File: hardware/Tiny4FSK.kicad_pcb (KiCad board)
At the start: 4 copper layers, 18 x 63 mm, 88 parts, among them J10 GPIO_ROW, J2 PWR, J7 GCT-4105, J8 SWD, J9 Counterpoise, SW1 PWR, SW2 RST, U1 BME280, U10 USBLC6-2SC6, U11 ATGM336H, U3 TPS61200DRC, U5 ATSAMD21G18A-A, U6 Si4463, U7 XC6210B332MR, U9 TPS2116DRL

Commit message: more layout progress
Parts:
- moved C30 6.01 mm to (145.6, 97.1)
- moved U2 5.48 mm to (143.8, 96.7), turned to 90 degrees
- moved AE1 3.29 mm to (146.1, 65.9), turned to 180 degrees
- moved R7 0.64 mm to (147.8, 86.1), turned to 135 degrees
- moved J7 0.55 mm to (145.9, 103.5)
- moved L8 0.52 mm to (151.8, 65.9)
- moved R22 0.50 mm to (147.9, 96.8), turned to 45 degrees
- moved R8 0.45 mm to (156.1, 87.5), turned to -135 degrees
- moved U8 0.40 mm to (150.6, 110.5)
- moved C26 0.40 mm to (150.6, 112.4)
- moved R9 0.29 mm to (155.4, 86.8)
- moved C9 0.11 mm to (146.5, 87.4)
- moved C11 0.11 mm to (147.1, 86.8)
- moved C37 0.06 mm to (144.6, 93.5)
- moved R21 0.06 mm to (145.3, 94.2)

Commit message: draft of routing
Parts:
- removed J9: Counterpoise, Connector_PinHeader_2.54mm:PinHeader_1x01_P2.54mm_Vertical
- moved H2 50.2 mm to (158.8, 120.8)
- moved H1 17.6 mm to (158.8, 70.2)
- moved C34 8.72 mm to (152.6, 114.4)
- moved C35 8.72 mm to (151.7, 114.4)
- moved C25 7.37 mm to (150.2, 115.1), turned to 0 degrees
- moved U9 4.21 mm to (149.9, 113.2), turned to -90 degrees
- moved C19 3.79 mm to (147.6, 112.1), turned to 180 degrees
- moved C26 3.33 mm to (148.4, 109.9), turned to 90 degrees
- moved AE1 3.22 mm to (144.1, 68.4), turned to -90 degrees
- moved L3 2.18 mm to (156.6, 112.2)
- moved R5 1.14 mm to (151.2, 101.0)
- moved C18 1.13 mm to (156.4, 97.8)
- moved C17 1.03 mm to (151.3, 98.6)
- moved U7 1.03 mm to (153.9, 99.1)
- moved U10 1.01 mm to (153.8, 102.5)
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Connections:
- C27 pad 2: /radio/SI_TX -> Net-(C16-Pad2)
- J10 pad 10: /interface/GP.GPIO13 -> /interface/GP.GPIO10
- J10 pad 11: /interface/GP.GPIO38 -> /interface/GP.GPIO12
- J10 pad 13: /interface/GP.GPIO_A_1 -> /interface/GP.SCL
- J10 pad 14: /interface/GP.GPIO_A_2 -> /interface/GP.SDA
- J10 pad 2: /interface/GP.SDA -> /interface/GP.GPIO_A_1
- J10 pad 3: /interface/GP.SCL -> /interface/GP.GPIO_A_2
- J10 pad 9: /interface/GP.GPIO12 -> /interface/GP.GPIO13
- J2 pad 2: +BATT -> +3.3V
- J2 pad 6: +3.3V -> +BATT
- L10 pad 2: /radio/SI_TX -> Net-(C16-Pad2)
- U5 pad 11: /mcu/GPS.EN -> /mcu/SI.SDN
- U5 pad 13: /interface/LED.SUCCESS -> /interface/GP.~{CS}
- U5 pad 14: /mcu/SI_CTL.GP1 -> /mcu/SI.GP1
- U5 pad 22: /interface/GP.GPIO38 -> /mcu/SI.GP0
- U5 pad 23: /mcu/SI.GP0 -> unconnected-(U5-PA14-Pad23)
- U5 pad 24: /interface/LED.ERROR -> unconnected-(U5-PA15-Pad24)
- U5 pad 25: /mcu/SI.SDN -> unconnected-(U5-PA16-Pad25)
- U5 pad 27: /interface/GP.~{CS} -> /interface/GP.GPIO10
- U5 pad 39: unconnected-(U5-PA27-Pad39) -> /mcu/GPS.EN
- U5 pad 47: unconnected-(U5-PB02-Pad47) -> /interface/LED.SUCCESS
- U5 pad 48: unconnected-(U5-PB03-Pad48) -> /interface/LED.ERROR
- U6 pad 14: /interface/GP.MISO -> /interface/GP.MOSI
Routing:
- net +BATT: track 0.00 -> 60.7 mm, vias 0 -> 6
- net /interface/PROG.~{RESET}: track 0.00 -> 52.1 mm, vias 0 -> 2
- net /interface/GP.GPIO_A_1: track 0.00 -> 40.9 mm, vias 0 -> 1
- net /interface/GP.GPIO_A_2: track 0.00 -> 39.1 mm, vias 0 -> 1
- net /interface/LED.SUCCESS: track 0.00 -> 38.6 mm, vias 0 -> 2
- net /interface/LED.ERROR: track 0.00 -> 37.1 mm, vias 0 -> 2
- net +3.3V: track 0.00 -> 36.7 mm, vias 0 -> 24
- net /interface/GP.SDA: track 0.00 -> 26.0 mm, vias 0 -> 1
- net /interface/GP.SCL: track 0.00 -> 24.6 mm
- net /power/USB_3V3: track 0.00 -> 23.9 mm, vias 0 -> 3
- net /interface/GP.MISO: track 0.00 -> 22.9 mm, vias 0 -> 3
- net /interface/GP.MOSI: track 0.00 -> 22.6 mm, vias 0 -> 2
- net /power/USB_VBUS: track 0.00 -> 21.7 mm, vias 0 -> 9
- net /interface/GP.D+: track 0.00 -> 21.5 mm, vias 0 -> 2
- net /power/BST_IN: track 0.00 -> 20.2 mm, vias 0 -> 5
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- added copper zone on F.Cu, net +3.3V
- added copper zone on In2.Cu, net +3.3V
- added copper zone on In2.Cu, net /power/BATT_3V3
- added copper zone on F.Cu, net /power/BST_IN
- added copper zone on In2.Cu, net /power/USB_VBUS
- added copper zone on B.Cu, net Earth
- added copper zone on F.Cu, net Earth
- added copper zone on In1.Cu, net Earth
- added copper zone on F.Cu, net Net-(U3-L)

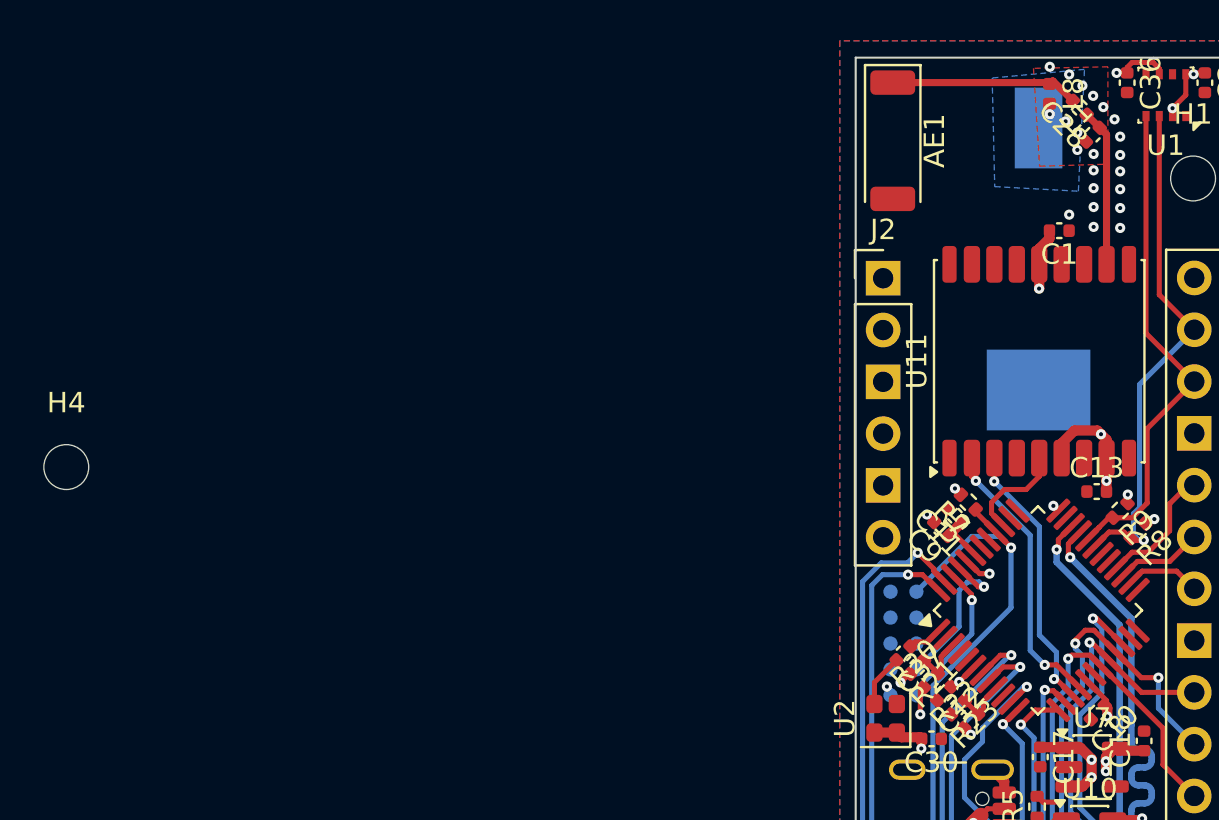
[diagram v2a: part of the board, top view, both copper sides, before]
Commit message: fix footprints
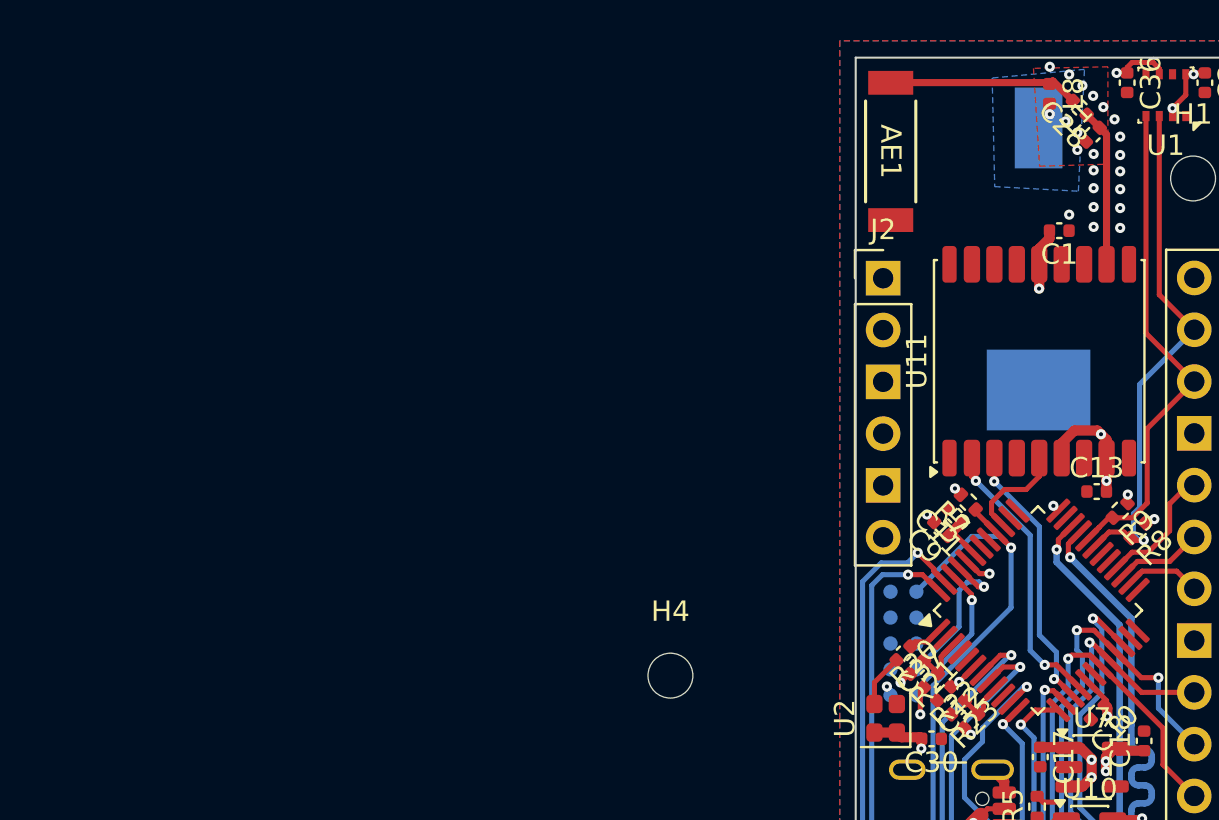
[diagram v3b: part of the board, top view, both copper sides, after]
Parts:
- AE1: footprint RF_Antenna:Johanson_2450AT43F0100_2400-2500Mhz -> RF_Antenna_Custom:ANT_1575AT_JOT
- moved H4 31.3 mm to (133.2, 94.6)
- moved AE1 0.53 mm to (144.0, 68.9)
